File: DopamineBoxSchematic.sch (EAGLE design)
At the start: 47 parts, among them U1 ARDUINOR3-BPLACE

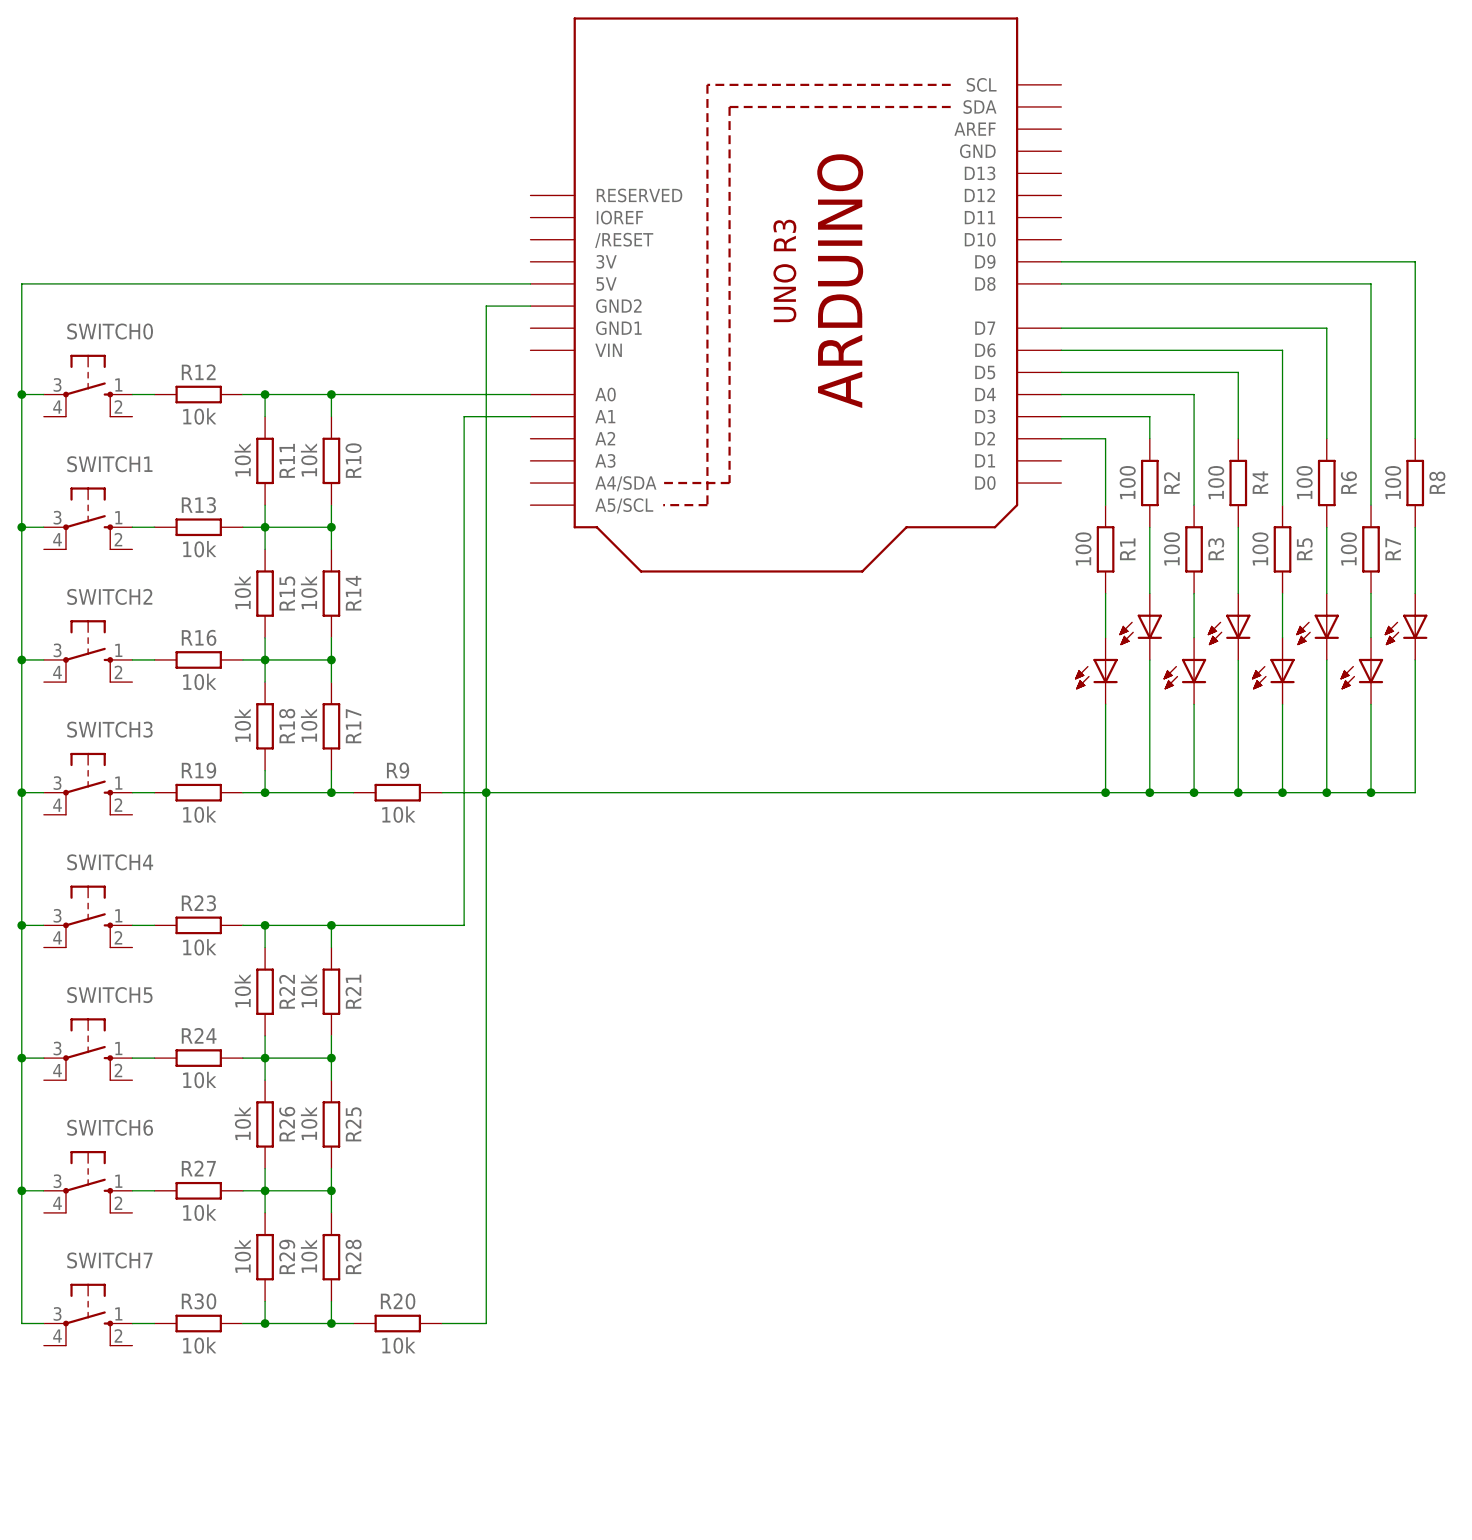
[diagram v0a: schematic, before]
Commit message: switches have to actually switch to GND (cannot leave input floating and cannot us a pulldown either as it would influence the R-2R ladder)
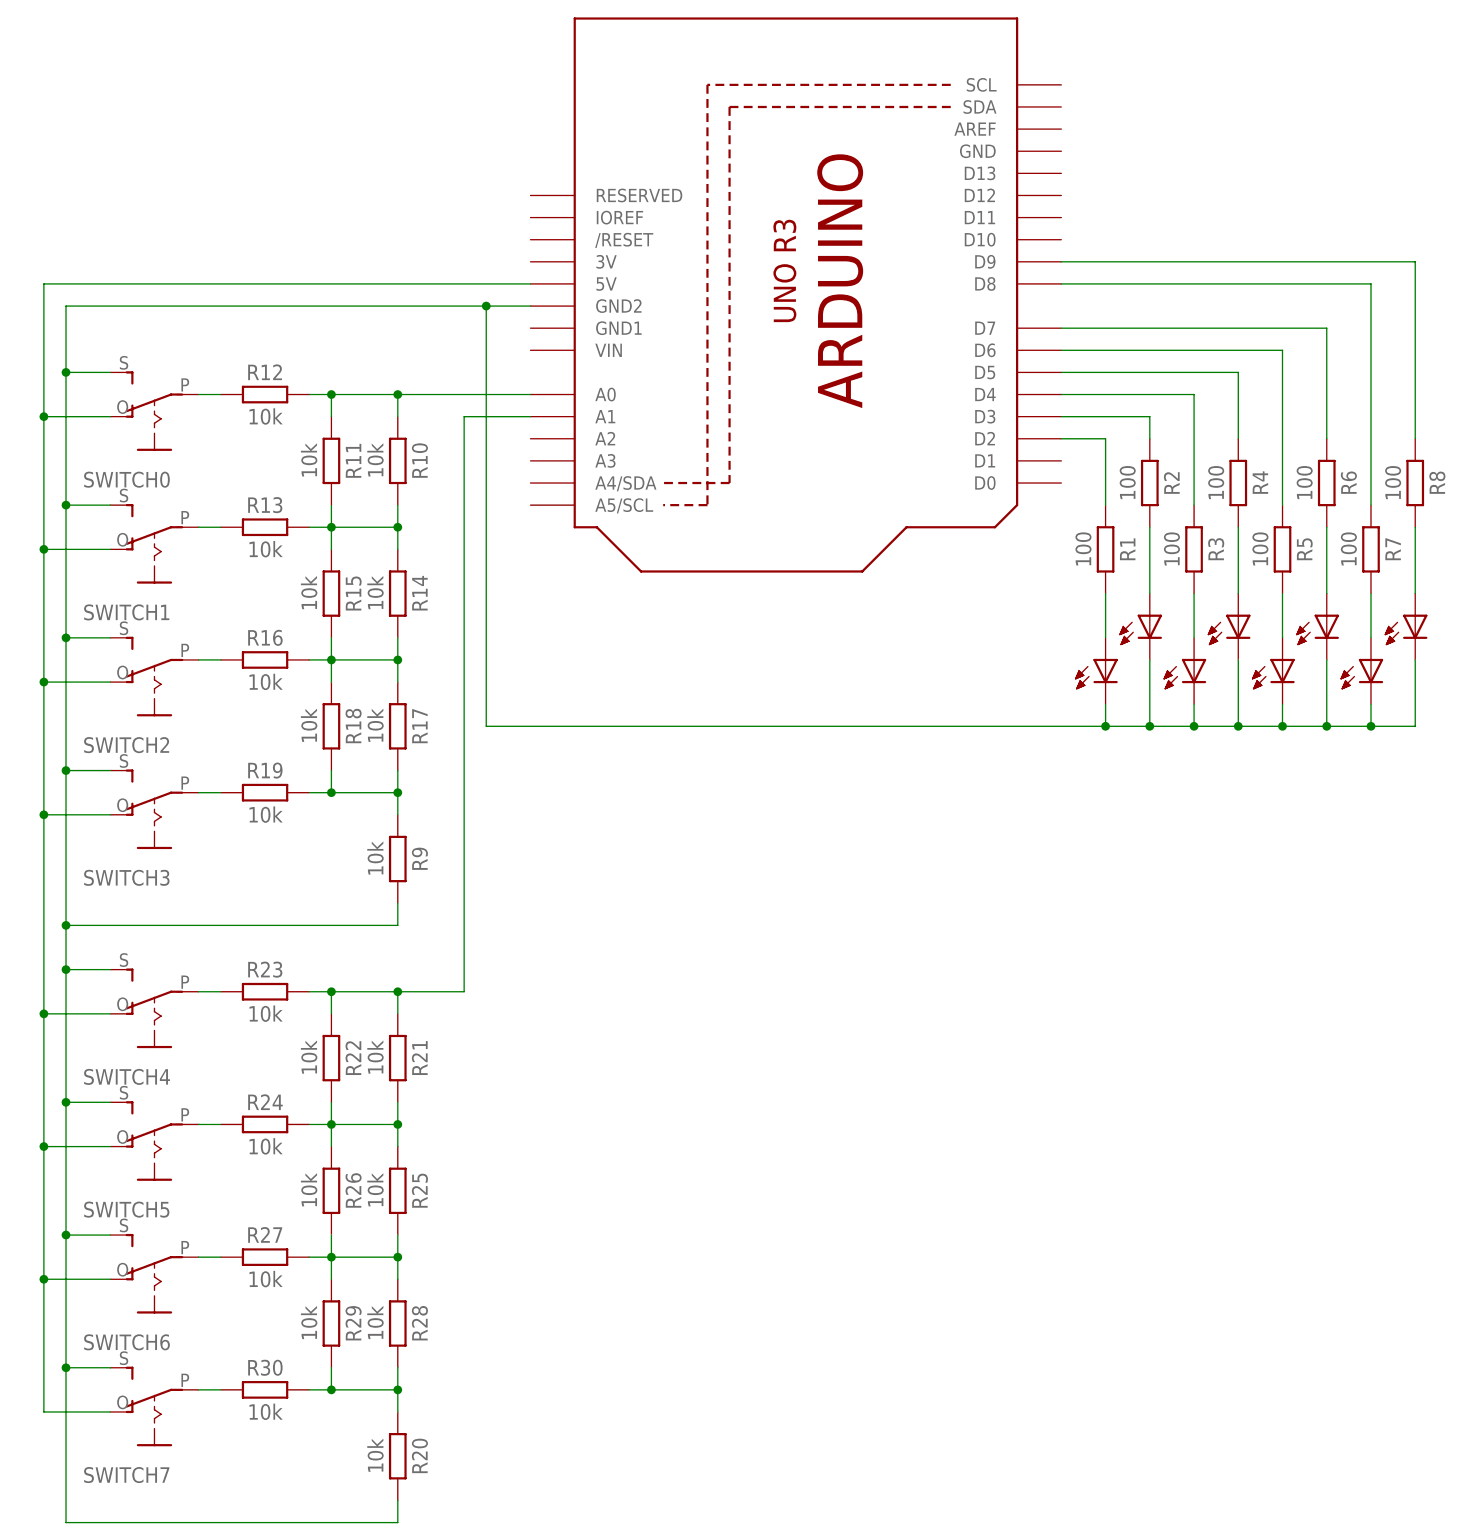
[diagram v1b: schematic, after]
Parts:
- SWITCH0, SWITCH1, SWITCH2, SWITCH3, SWITCH4, SWITCH5, SWITCH6, SWITCH7: device adafruit:40-XX-ROUND -> adafruit:EG1218S
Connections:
- removed net N$26: LED0.C, LED2.C, LED3.C, LED4.C, LED5.C, LED6.C, LED7.C, LED8.C, R20.2, R9.2, U1.GND2
- removed net N$27: SWITCH0.P, SWITCH1.P, SWITCH2.P, SWITCH3.P, SWITCH4.P, SWITCH5.P, SWITCH6.P, SWITCH7.P, U1.5V
- new net N$21: LED0.C, LED2.C, LED3.C, LED4.C, LED5.C, LED6.C, LED7.C, LED8.C, R20.2, R9.2, SWITCH0.S, SWITCH1.S, SWITCH2.S, SWITCH3.S, SWITCH4.S, SWITCH5.S, SWITCH6.S, SWITCH7.S, U1.GND2
- new net N$44: SWITCH0.O, SWITCH1.O, SWITCH2.O, SWITCH3.O, SWITCH4.O, SWITCH5.O, SWITCH6.O, SWITCH7.O, U1.5V
- net N$22: now also SWITCH0.P; no longer SWITCH0.S
- net N$23: now also SWITCH1.P; no longer SWITCH1.S
- net N$24: now also SWITCH2.P; no longer SWITCH2.S
- net N$25: now also SWITCH3.P; no longer SWITCH3.S
- net N$32: now also SWITCH4.P; no longer SWITCH4.S
- net N$33: now also SWITCH5.P; no longer SWITCH5.S
- net N$34: now also SWITCH6.P; no longer SWITCH6.S
- net N$35: now also SWITCH7.P; no longer SWITCH7.S
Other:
- moved on the sheet: R10, R11, R12, R13, R14, R15, R16, R17, R18, R19, R20, R21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
